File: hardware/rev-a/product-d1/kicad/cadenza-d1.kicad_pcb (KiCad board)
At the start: 4 copper layers, 116 x 64 mm, 65 parts, among them J1 USB-C USB2 Sink, J2 LS027B7DH01 FPC, J3 microSD push-push, J4 LiPo 1S, J5 Speaker 8R 1-2W, J6 Encoder daughterboard, SW1 POWER RUN/OFF, SW2 B, SW3 MENU, SW4 RESET, SW5 BOOT, U1 ESP32-S3-WROOM-1-N16R8, U2 BQ24074RGTR, U3 TPS63070RNMR, U4 TPS61023DRLR, U5 MAX98357AETE+T, U6 IM73D122V01, U7 BQ27441DRZR-G1A, U8 USBLC6-2SC6

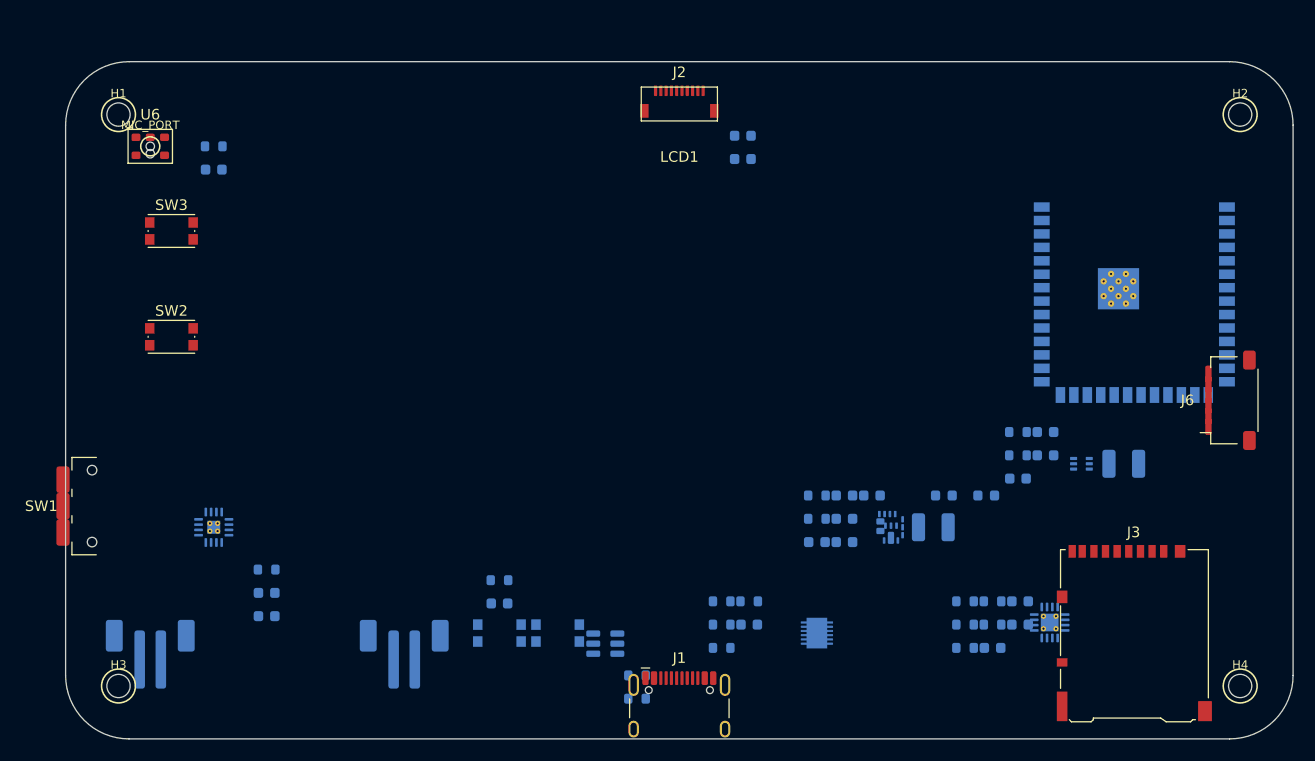
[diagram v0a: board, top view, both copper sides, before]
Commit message: wip: add capability mode JSON, update circuit and component documentation for Rev A
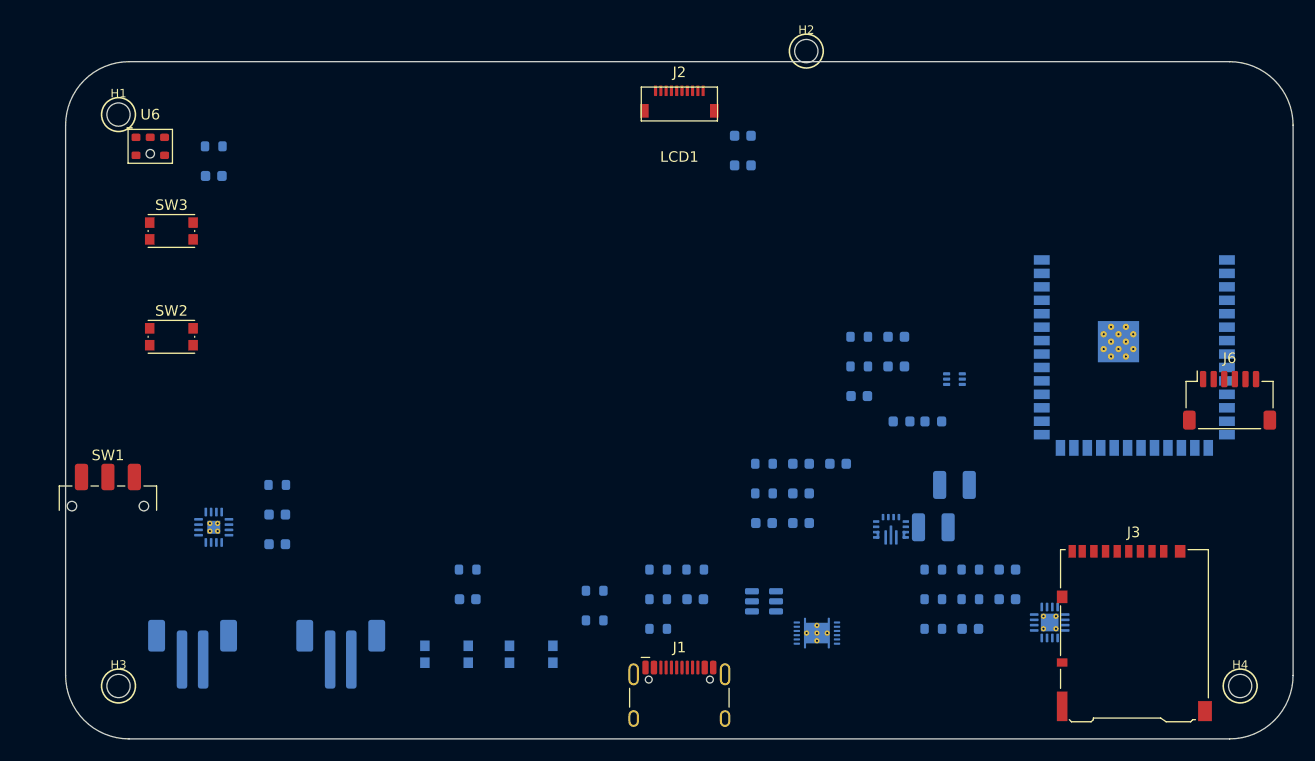
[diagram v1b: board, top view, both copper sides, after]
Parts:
- removed MIC_PORT: NPTH 0.8mm, Cadenza_D1:MIC_PORT
- U3: footprint Cadenza_D1:TI_RNM0015A_VQFN-HR-15_2.5x3mm -> Cadenza_D1:TI_RNM0015A_VQFN-HR-15_TI4222000B
- U7: footprint Cadenza_D1:TI_DRZ0012A_VSON-12_2.5x4mm -> Package_SON:Texas_S-PDSO-N12
- moved H2 41.4 mm to (120.0, 49.0)
- moved R20 17.5 mm to (125.0, 76.0)
- moved R21 17.2 mm to (125.0, 78.8)
- moved C20 16.9 mm to (125.0, 81.6)
- moved C21 16.7 mm to (128.5, 76.0)
- moved C22 16.4 mm to (128.5, 78.8)
- moved L2 16.1 mm to (134.0, 90.0)
- moved U8 15.5 mm to (116.0, 101.0)
- moved U4 14.4 mm to (134.0, 80.0)
- moved R1 8.94 mm to (100.0, 100.0)
- moved FB1 8.60 mm to (132.0, 84.0)
- moved R2 8.41 mm to (100.0, 102.8)
- moved FB2 8.06 mm to (129.0, 84.0)
- moved R41 8.06 mm to (70.0, 90.0)
- moved C50 7.47 mm to (70.0, 92.8)
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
